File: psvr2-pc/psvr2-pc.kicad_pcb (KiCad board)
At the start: 4 copper layers, 101.3 x 63.5 mm, 109 parts, among them IC1 SN65MLVD200D, IC2 SN65MLVD200D, J1 USB_C_Receptacle, J2 USB3_B_Micro, J3 DP_47272, J4 Barrel_Jack_Switch, J5 Conn_01x02_Pin, Q1 Si2301CDS, Q2 PN2222A, Q3 Si2301CDS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

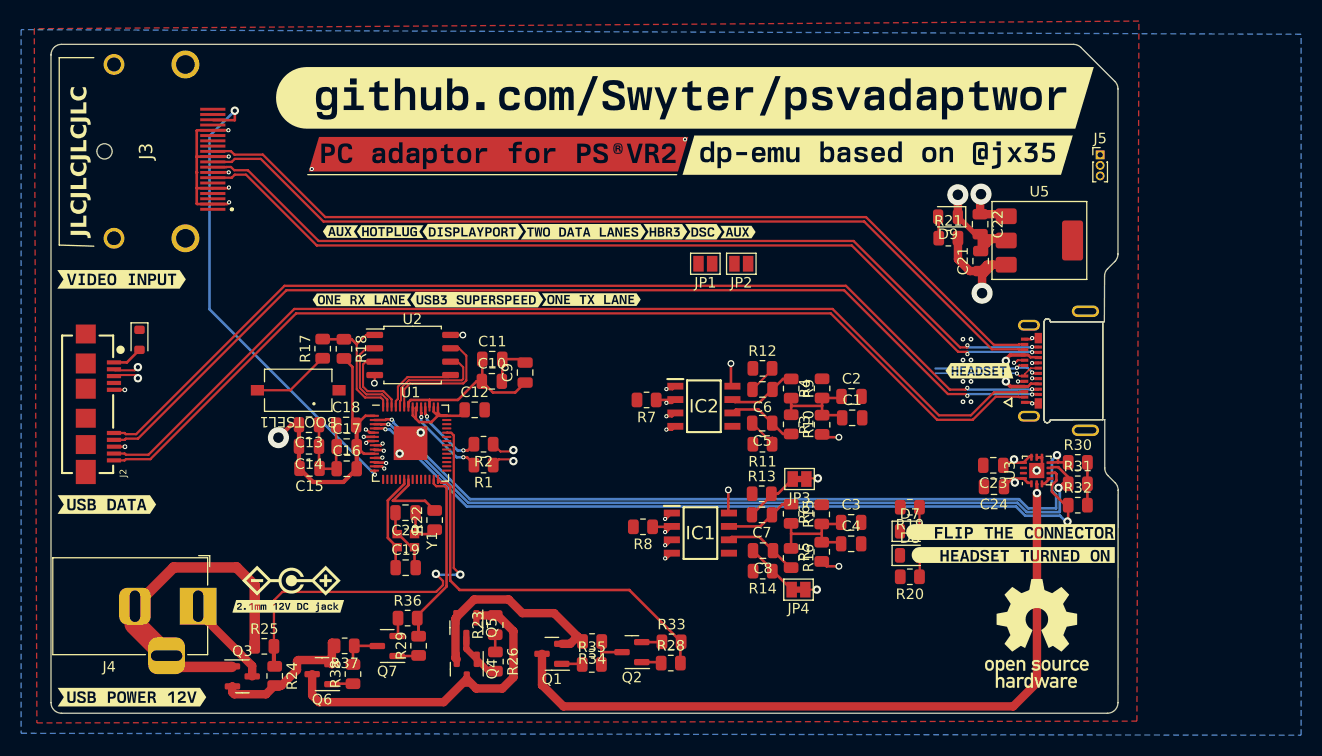
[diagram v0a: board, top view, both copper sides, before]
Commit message: Try to route the DP-AUX pair around somewhere useful without taking them over separate ways, they use differential signaling (albeit slow) and are AC coupled, I think.
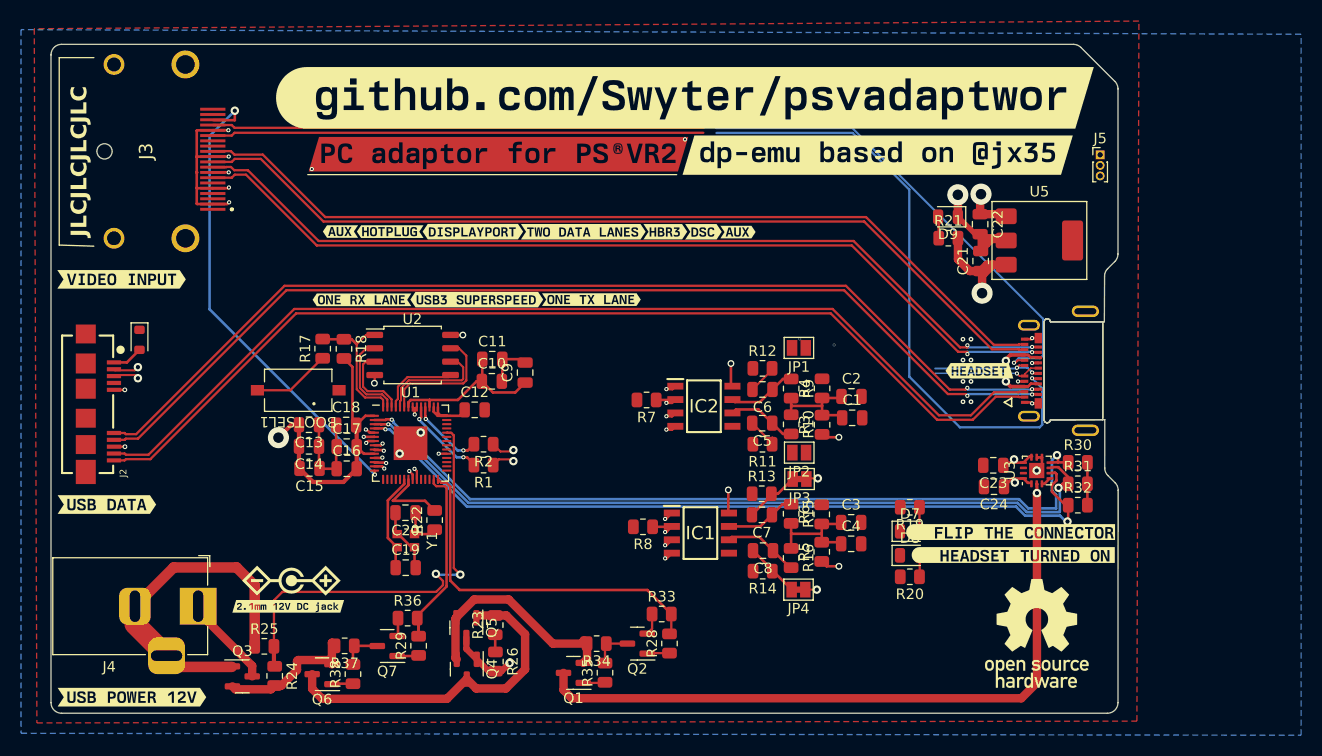
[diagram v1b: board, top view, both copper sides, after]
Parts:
- moved JP2 18.8 mm to (83.7, 51.5)
- moved JP1 11.9 mm to (83.7, 41.5)
- moved R33 2.80 mm to (70.7, 66.8)
- moved Q1 2.73 mm to (62.3, 72.4)
- moved R28 1.86 mm to (71.4, 69.6), turned to 90 degrees
- moved R35 1.48 mm to (65.3, 72.4), turned to 90 degrees
- moved Q2 0.96 mm to (68.4, 69.6)
- moved R34 0.48 mm to (64.5, 69.6)
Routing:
- net /HMD_AUX_N: track 1.68 -> 59.5 mm, vias 2 -> 3
- net /PC_AUX_N: track 2.87 -> 49.9 mm
- net /PC_AUX_P: track 2.77 -> 49.5 mm
- net /HMD_AUX_P: track 2.23 -> 47.4 mm, vias 2 -> 3
- net /HMD_VBUS: track 92.5 -> 88.3 mm
- net /HMD_ENABLE_VBUS: track 36.8 -> 34.6 mm
- net /PC_VBUS_5V: track 9.21 -> 10.9 mm, vias 1 -> 2
- net +3.3V: track 62.8 -> 61.2 mm, vias 7 -> 10
- net Net-(Q1-S): track 20.2 -> 21.3 mm
- net +1V1: track 16.0 -> 17.1 mm, vias 0 -> 1
- net /VBUS_12V: track 31.7 -> 32.7 mm
- net /DC_JACK_12V: track 14.6 -> 13.8 mm

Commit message: Making the AUX connections work, still kind of ugly, though.
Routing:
- net /HMD_AUX_N: track 59.5 -> 37.3 mm
- net /HMD_AUX_P: track 47.4 -> 49.3 mm
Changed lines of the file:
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@@
   (segment (start 65.2375 73.32) (end 65.2925 73.265) (width 0.2205) (layer "F.Cu") (net 56))
   (segment (start 63.23 73.32) (end 65.2375 73.32) (width 0.2205) (layer "F.Cu") (net 56))
-  (segment (start 104.230708 42.932895) (end 104.475603 42.688) (width 0.2) (layer "F.Cu") (net 57))
   (segment (start 84.476 53.9) (end 84.411 53.965) (width 0.2) (layer "F.Cu") (net 57))
-  (segment (start 104.475603 42.688) (end 105.13 42.688) (width 0.2) (layer "F.Cu") (net 57))
-  (segment (start 104.119211 42.932895) (end 104.230708 42.932895) (width 0.2) (layer "F.Cu") (net 57))
+  (segment (start 104.356212 42.688) (end 105.13 42.688) (width 0.2) (layer "F.Cu") (net 57))
+  (segment (start 104.116257 42.927955) (end 104.356212 42.688) (width 0.2) (layer "F.Cu") (net 57))
   (segment (start 85.5 53.9) (end 84.476 53.9) (width 0.2) (layer "F.Cu") (net 57))
   (via (at 85.5 53.9) (size 0.8) (drill 0.4) (layers "F.Cu" "B.Cu") (net 57))
-  (via (at 104.119211 42.932895) (size 0.4) (drill 0.2) (layers "F.Cu" "B.Cu") (net 57))
+  (via (at 104.116257 42.927955) (size 0.4) (drill 0.2) (layers "F.Cu" "B.Cu") (net 57))
   (via (at 83.79 40.67) (size 0.25) (drill 0.2) (layers "F.Cu" "B.Cu") (net 57))
-  (segment (start 75.88 20.65) (end 75.85 20.62) (width 0.2) (layer "B.Cu") (net 57))
-  (segment (start 106.875568 38.745568) (end 88.78 20.65) (width 0.2) (layer "B.Cu") (net 57))
-  (segment (start 104.119211 42.932895) (end 104.552106 42.5) (width 0.2) (layer "B.Cu") (net 57))
-  (segment (start 106.875568 42.224432) (end 106.875568 38.745568) (width 0.2) (layer "B.Cu") (net 57))
-  (segment (start 104.027105 42.932895) (end 104.01 42.95) (width 0.2) (layer "B.Cu") (net 57))
-  (segment (start 106.6 42.5) (end 106.875568 42.224432) (width 0.2) (layer "B.Cu") (net 57))
-  (segment (start 104.552106 42.5) (end 106.6 42.5) (width 0.2) (layer "B.Cu") (net 57))
-  (segment (start 104.119211 42.932895) (end 104.027105 42.932895) (width 0.2) (layer "B.Cu") (net 57))
-  (segment (start 88.78 20.65) (end 75.88 20.65) (width 0.2) (layer "B.Cu") (net 57))
+  (segment (start 104.116257 42.927955) (end 104.116257 42.667728) (width 0.2) (layer "In2.Cu") (net 57))
+  (segment (start 104.116257 42.667728) (end 103.498529 42.05) (width 0.2) (layer "In2.Cu") (net 57))
+  (segment (start 102.27 50.33) (end 87.03 65.57) (width 0.2) (layer "In2.Cu") (net 57))
+  (segment (start 103.201471 42.05) (end 102.27 42.981471) (width 0.2) (layer "In2.Cu") (net 57))
+  (segment (start 85.5 54.86) (end 85.5 53.9) (width 0.2) (layer "In2.Cu") (net 57))
+  (segment (start 102.27 42.981471) (end 102.27 50.33) (width 0.2) (layer "In2.Cu") (net 57))
+  (segment (start 87.03 65.57) (end 84.01 65.57) (width 0.2) (layer "In2.Cu") (net 57))
+  (segment (start 84.01 65.57) (end 84.01 56.35) (width 0.2) (layer "In2.Cu") (net 57))
+  (segment (start 103.498529 42.05) (end 103.201471 42.05) (width 0.2) (layer "In2.Cu") (net 57))
+  (segment (start 84.01 56.35) (end 85.5 54.86) (width 0.2) (layer "In2.Cu") (net 57))
+  (segment (start 104.032045 42.927955) (end 104.01 42.95) (width 0.2) (layer "B.Cu") (net 57))
+  (segment (start 104.116257 42.927955) (end 104.032045 42.927955) (width 0.2) (layer "B.Cu") (net 57))
   (segment (start 85.4 64.465) (end 84.311 64.465) (width 0.2) (layer "F.Cu") (net 58))
-  (segment (start 106.43 44.438) (end 105.888003 44.438) (width 0.2) (layer "F.Cu") (net 58))
-  (segment (start 105.888003 44.438) (end 105.85 44.399997) (width 0.2) (layer "F.Cu") (net 58))
-  (via (at 105.841116 44.399997) (size 0.4) (drill 0.2) (layers "F.Cu" "B.Cu") (net 58))
+  (segment (start 106.391997 44.399997) (end 105.85 44.399997) (width 0.2) (layer "F.Cu") (net 58))
+  (segment (start 106.43 44.438) (end 106.391997 44.399997) (width 0.2) (layer "F.Cu") (net 58))
+  (via (at 105.85 44.399997) (size 0.4) (drill 0.2) (layers "F.Cu" "B.Cu") (net 58))
   (via (at 85.4 64.465) (size 0.8) (drill 0.4) (layers "F.Cu" "B.Cu") (net 58))
   (via (at 87.04 41.24) (size 0.25) (drill 0.2) (layers "F.Cu" "B.Cu") (net 58))
-  (segment (start 94.18 26.48876) (end 88.80124 21.11) (width 0.2205) (layer "B.Cu") (net 58))
-  (segment (start 98.99 49.06) (end 94.18 44.25) (width 0.2205) (layer "B.Cu") (net 58))
-  (segment (start 106.55 49.06) (end 98.99 49.06) (width 0.2205) (layer "B.Cu") (net 58))
-  (segment (start 94.18 44.25) (end 94.18 26.48876) (width 0.2205) (layer "B.Cu") (net 58))
-  (segment (start 105.841116 44.399997) (end 106.80025 45.359131) (width 0.2205) (layer "B.Cu") (net 58))
-  (segment (start 106.80025 45.359131) (end 106.80025 48.80975) (width 0.2205) (layer "B.Cu") (net 58))
-  (segment (start 106.80025 48.80975) (end 106.55 49.06) (width 0.2205) (layer "B.Cu") (net 58))
-  (segment (start 88.80124 21.11) (end 75.87 21.11) (width 0.2205) (layer "B.Cu") (net 58))
+  (segment (start 101.95975 42.852961) (end 101.95975 50.20149) (width 0.2205) (layer "In2.Cu") (net 58))
+  (segment (start 103.072961 41.73975) (end 101.95975 42.852961) (width 0.2205) (layer "In2.Cu") (net 58))
+  (segment (start 87.710736 64.465) (end 101.95975 50.215986) (width 0.2) (layer "In2.Cu") (net 58))
+  (segment (start 105.740221 44.399997) (end 104.86 43.519776) (width 0.2205) (layer "In2.Cu") (net 58))
+  (segment (start 104.86 43.519776) (end 104.86 42.96) (width 0.2205) (layer "In2.Cu") (net 58))
+  (segment (start 101.95975 50.215986) (end 101.95975 50.20149) (width 0.2) (layer "In2.Cu") (net 58))
+  (segment (start 103.63975 41.73975) (end 103.072961 41.73975) (width 0.2205) (layer "In2.Cu") (net 58))
+  (segment (start 105.85 44.399997) (end 105.740221 44.399997) (width 0.2205) (layer "In2.Cu") (net 58))
+  (segment (start 104.86 42.96) (end 103.63975 41.73975) (width 0.2205) (layer "In2.Cu") (net 58))
+  (segment (start 85.4 64.465) (end 87.710736 64.465) (width 0.2) (layer "In2.Cu") (net 58))
   (segment (start 81.155 43.4625) (end 81.155 43.6) (width 0.2) (layer "F.Cu") (net 60))
   (segment (start 29.860001 21.36) (end 30.124751 21.09525) (width 0.2205) (layer "F.Cu") (net 60))

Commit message: More changes, I honestly forgot what.
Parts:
- moved JP2 5.12 mm to (88.7, 52.6)
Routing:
- net /HMD_USB2_N: track 10.9 -> 67.4 mm, vias 2 -> 3
- net /HMD_USB2_P: track 10.3 -> 66.8 mm, vias 1 -> 2
- net /PC_AUX_N: track 49.9 -> 89.0 mm, vias 0 -> 3
- net /PC_AUX_P: track 49.5 -> 78.9 mm, vias 0 -> 2
- net /DC_JACK_VOLT_SENSE: track 40.9 -> 42.0 mm
- net /HMD_AUX_P: track 49.3 -> 48.2 mm
- net /HMD_AUX_N: track 37.3 -> 38.0 mm, vias 3 -> 2

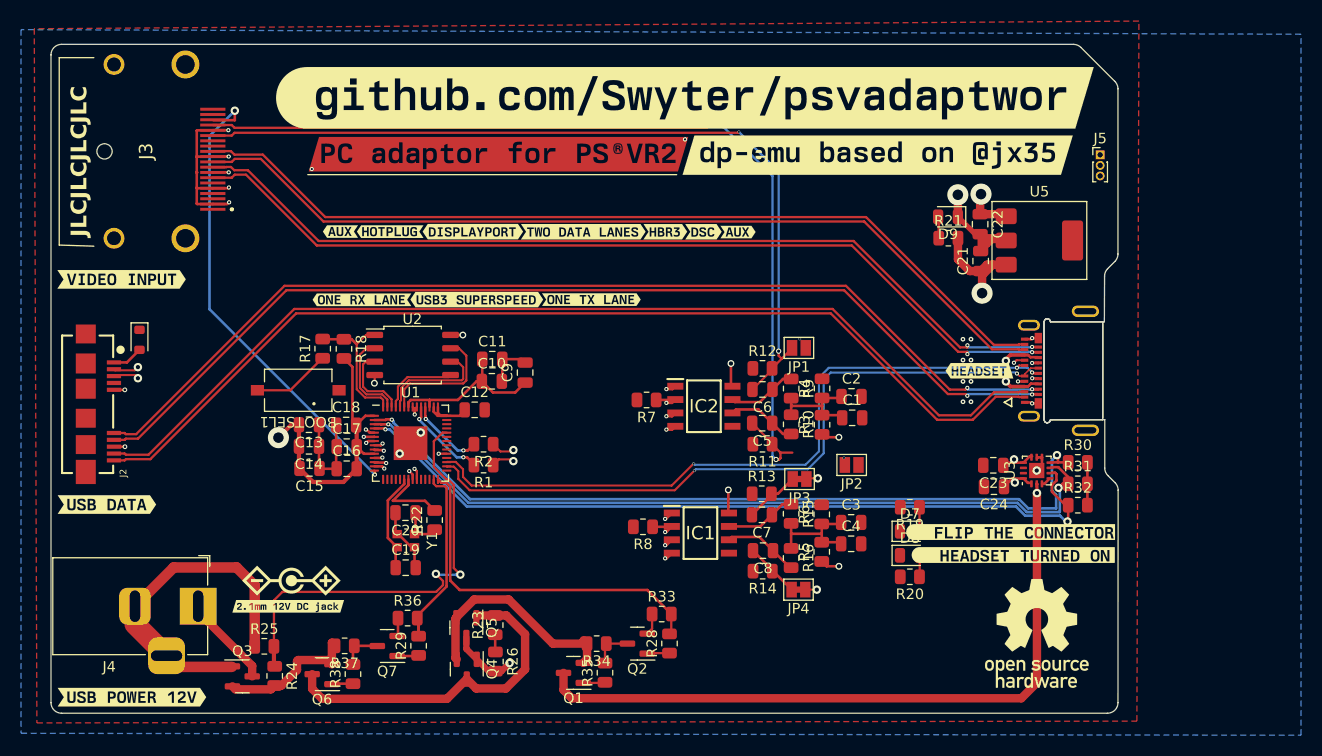
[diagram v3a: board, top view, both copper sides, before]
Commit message: Fix the VBUS_5V net not getting renamed into the PCB editor from the schematic due to an error with the diode footprint. Change it and now it works. Add the 5V power traces and keep connecting more stuff, only like 22 DRC problems found now. ¯\_(ツ)_/¯
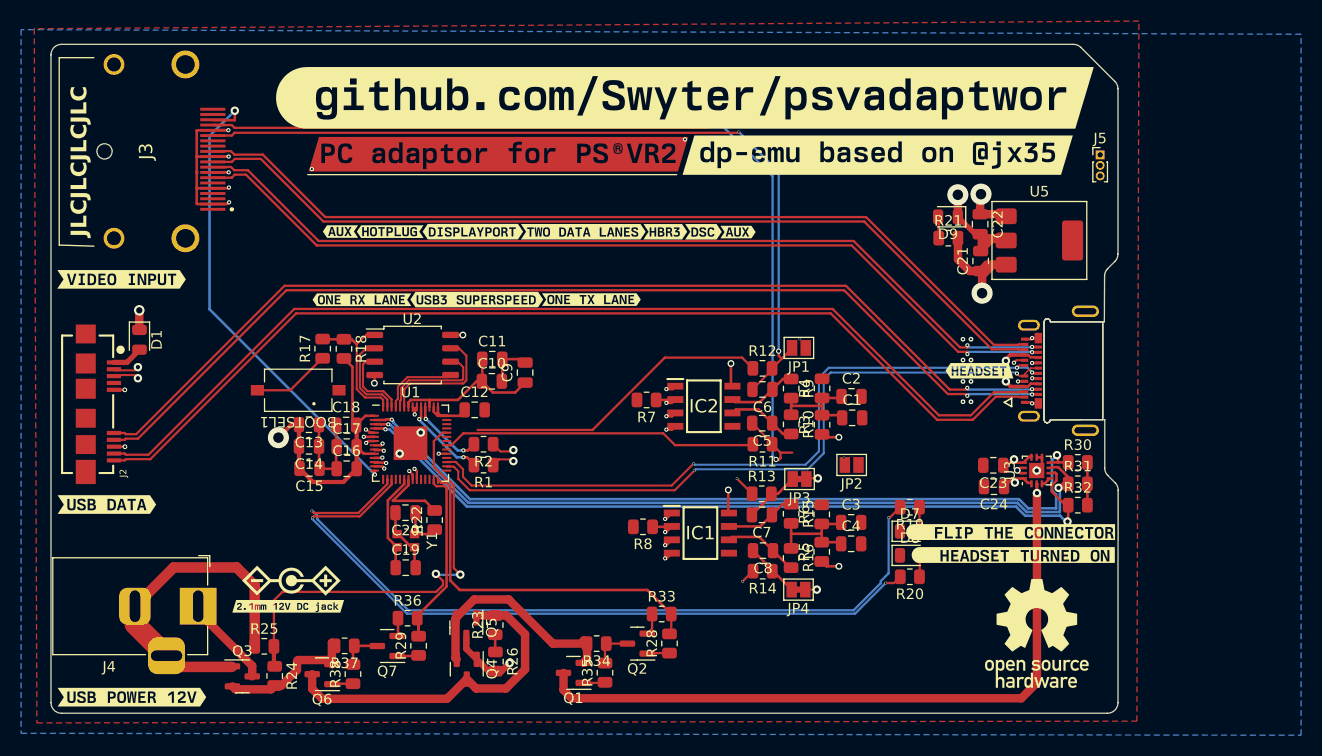
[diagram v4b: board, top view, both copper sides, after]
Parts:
- D1: value BAT54GWJ -> SS14; footprint Diode_SMD:D_SOD-110 -> Diode_SMD:D_0805_2012Metric
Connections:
- net Net-(J5-Pin_2) renamed /SWD
- net Net-(J5-Pin_3) renamed /SWCLK
- D1 pad 1: /PC_VBUS -> /PC_VBUS_5V
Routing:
- net /PC_VBUS_5V: track 10.9 -> 162.2 mm, vias 2 -> 3
- net /LED_CONN_WRONG_ORIENT: track 0.00 -> 76.1 mm, vias 0 -> 2
- net /LED_HMD_IS_READY: track 0.00 -> 70.4 mm, vias 0 -> 2
- net /HMD_AUX_TERMINATION_N: track 0.00 -> 62.2 mm, vias 0 -> 1
- net /HMD_AUX_TERMINATION_P: track 0.00 -> 34.2 mm, vias 0 -> 1
- net /PC_AUX_TERMINATION_N: track 0.00 -> 30.0 mm
- net /PC_AUX_TERMINATION_P: track 0.00 -> 29.4 mm
- net +3.3V: track 61.2 -> 62.6 mm, vias 10 -> 11
- net /PC_LVDS_D: track 32.1 -> 33.0 mm
- net /PC_LVDS_~{RE}: track 37.9 -> 38.8 mm
- net /PC_LVDS_R: track 38.4 -> 39.3 mm
- net /PC_LVDS_DR: track 34.8 -> 35.7 mm

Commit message: More DRC fixes, make the default annular size 0.4mm instead of 0.25. I messed up and all the new vias had this, causing a bunch of regressions. Almost there. :)
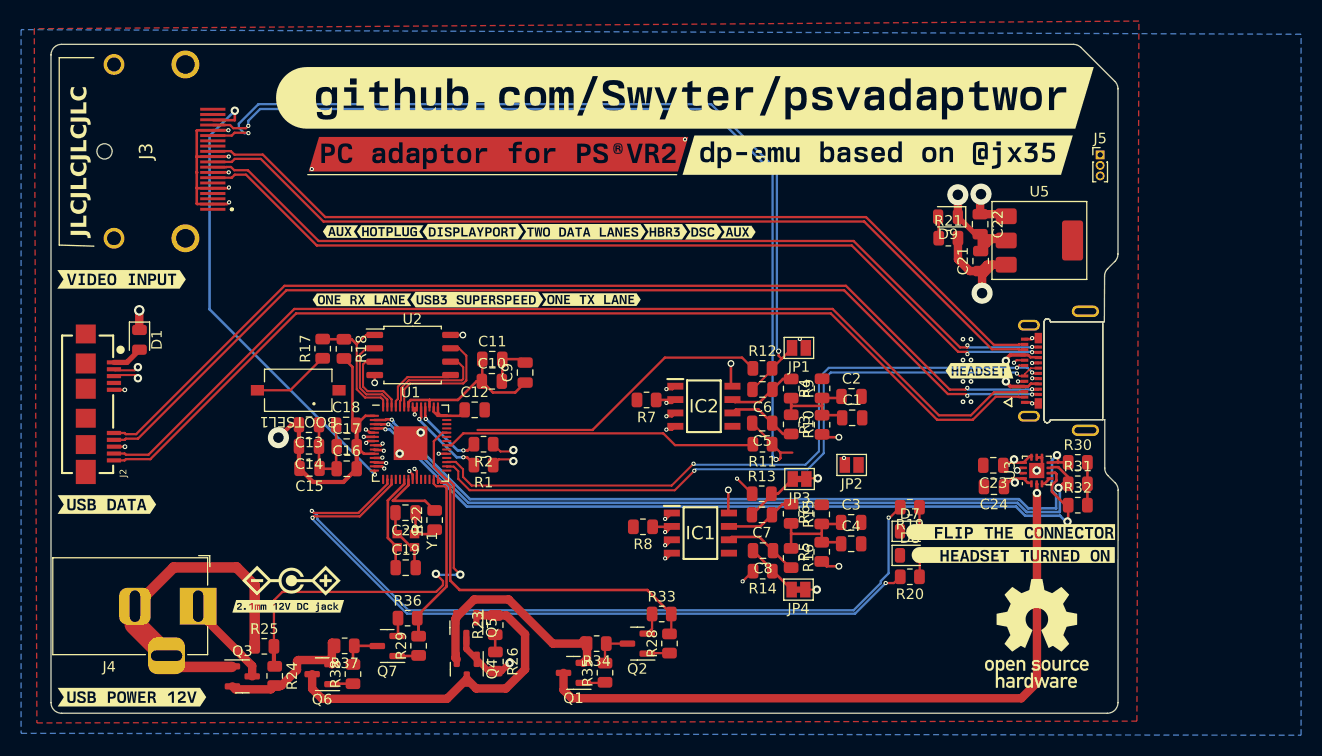
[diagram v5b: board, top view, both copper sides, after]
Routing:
- net /PC_AUX_P: track 78.9 -> 83.2 mm
- net /PC_AUX_N: track 89.0 -> 90.6 mm
